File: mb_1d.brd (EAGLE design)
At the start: 100 x 80 mm, 59 parts, among them CON1 1013279X_AMPHENOL_2X25, CON2 1013279X_AMPHENOL_2X25, U1 TPS61040, U10 TPS610981, U2 MAX5394, U3 TPS61040, U5 RFD77101, U6 MAX5394, U7 MAX5026EUT+T, U8 MAX5394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

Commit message: Ground pour completed
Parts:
- moved R26 1.64 mm to (52.1, 47.8)
- moved R11 0.75 mm to (71.6, 27.6), turned to 90 degrees
- moved R12 0.61 mm to (60.1, 54.7)
- moved C12 0.41 mm to (66.4, 27.6), turned to 270 degrees
- moved R10 0.17 mm to (68.8, 27.9)
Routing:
- net GND: track 0.00 -> 46.3 mm, vias 0 -> 24
- net SCK: track 46.8 -> 48.4 mm
- net FB: track 16.7 -> 15.4 mm
- net VLDO: track 3.35 -> 4.62 mm
- net SS_POT1: track 4.19 -> 5.30 mm
- net RSTB_M: track 37.8 -> 38.5 mm
- net SCK_LS: track 21.6 -> 22.1 mm
- net SDI_LS: track 24.2 -> 23.6 mm
- added copper zone on layer 1, net GND
- added copper zone on layer 16, net GND

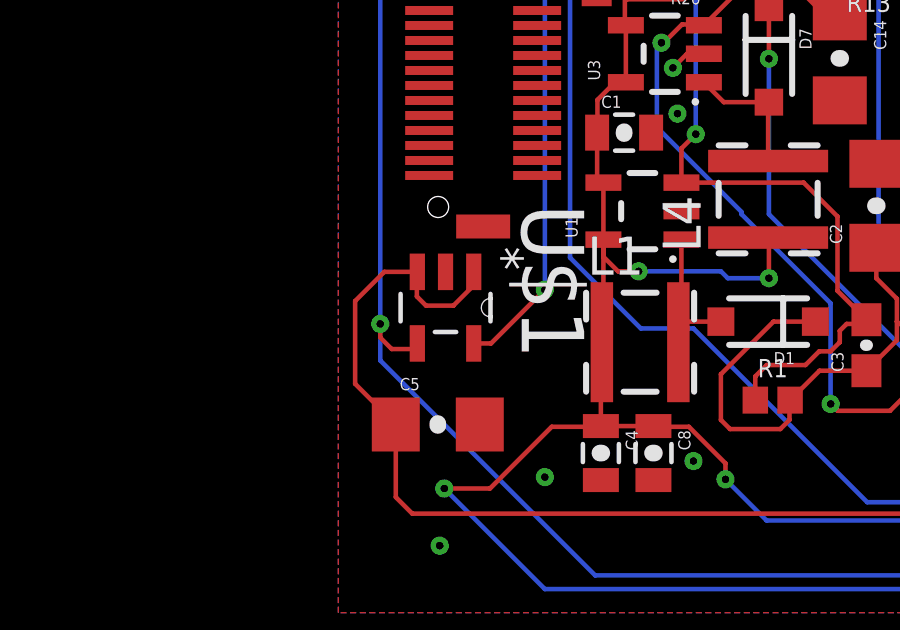
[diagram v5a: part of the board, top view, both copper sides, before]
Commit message: Fixed LT3014 error
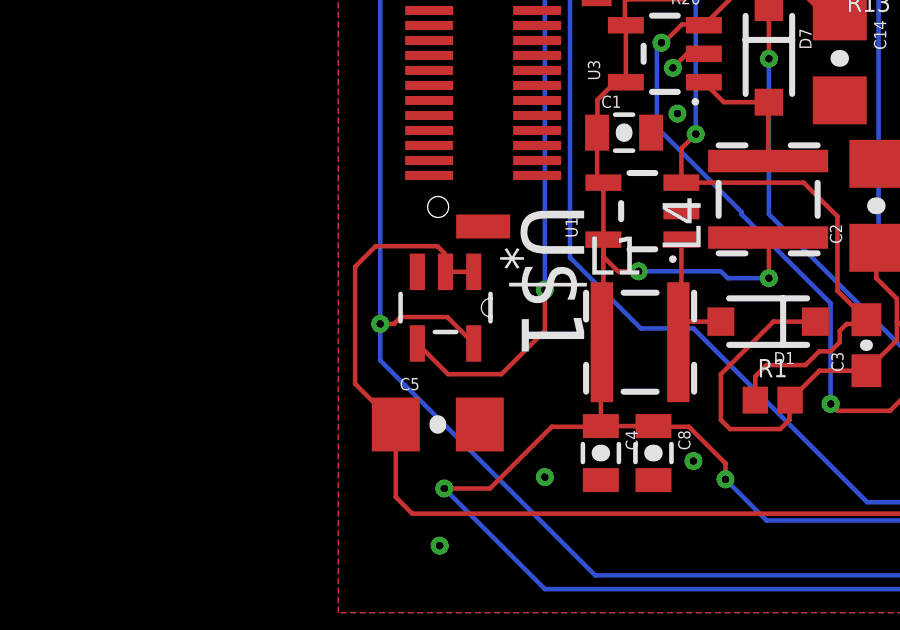
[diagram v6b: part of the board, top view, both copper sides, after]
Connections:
- net 50V: now also U$1.2; no longer U$1.3
- net ADJ: now also U$1.4; no longer U$1.5
- net GND: now also U$1.3; no longer U$1.2
- net HVDC: now also U$1.5; no longer U$1.4
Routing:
- net ADJ: track 37.4 -> 41.0 mm
- net HVDC: track 86.7 -> 88.3 mm
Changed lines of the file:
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@@
 <contactref element="U2" pad="2"/>
 <contactref element="R2" pad="1"/>
-<contactref element="U$1" pad="2"/>
+<contactref element="U$1" pad="3"/>
 <contactref element="C5" pad="2"/>
 <contactref element="U6" pad="2"/>
@@
 <signal name="HVDC">
 <contactref element="CON2" pad="32"/>
-<contactref element="U$1" pad="4"/>
+<contactref element="U$1" pad="5"/>
 <contactref element="R8" pad="1"/>
 <contactref element="C17" pad="2"/>
@@
 <wire x1="42.291" y1="55.245" x2="42.291" y2="36.0426" width="0.1524" layer="16"/>
 <via x="42.291" y="36.0426" extent="1-16" drill="0.254" diameter="0.381"/>
-<wire x1="42.291" y1="36.0426" x2="42.291" y2="35.5854" width="0.1524" layer="1"/>
-<wire x1="42.291" y1="35.5854" x2="42.672" y2="35.2044" width="0.1524" layer="1"/>
-<wire x1="42.672" y1="35.2044" x2="43.34" y2="35.2044" width="0.1524" layer="1"/>
-<wire x1="43.34" y1="35.2044" x2="43.5265" y2="35.3909" width="0.1524" layer="1"/>
 <wire x1="46.6132" y1="57.2516" x2="46.6132" y2="55.9435" width="0.1524" layer="1"/>
 <wire x1="46.6132" y1="55.9435" x2="46.5878" y2="55.9181" width="0.1524" layer="1"/>
@@
 <wire x1="49.4538" y1="27.6606" x2="42.291" y2="34.8234" width="0.1524" layer="16"/>
 <wire x1="42.291" y1="34.8234" x2="42.291" y2="36.0426" width="0.1524" layer="16"/>
+<wire x1="42.291" y1="36.0426" x2="42.7482" y2="36.0426" width="0.1524" layer="1"/>
+<wire x1="42.7482" y1="36.0426" x2="42.9768" y2="36.2712" width="0.1524" layer="1"/>
+<wire x1="42.9768" y1="36.2712" x2="44.5258" y2="36.2712" width="0.1524" layer="1"/>
+<wire x1="44.5258" y1="36.2712" x2="45.4061" y2="35.3909" width="0.1524" layer="1"/>
 </signal>
 <signal name="RESET">
@@
 <contactref element="R5" pad="2"/>
 <contactref element="U$1" pad="1"/>
-<contactref element="U$1" pad="3"/>
+<contactref element="U$1" pad="2"/>
 <contactref element="C5" pad="1"/>
 <wire x1="45.4061" y1="37.7785" x2="45.4061" y2="37.3289" width="0.1524" layer="1"/>
-<wire x1="45.4061" y1="37.3289" x2="44.7294" y2="36.6522" width="0.1524" layer="1"/>
-<wire x1="44.7294" y1="36.6522" x2="43.815" y2="36.6522" width="0.1524" layer="1"/>
-<wire x1="43.815" y1="36.6522" x2="43.5102" y2="36.957" width="0.1524" layer="1"/>
-<wire x1="43.5102" y1="36.957" x2="43.5102" y2="37.7622" width="0.1524" layer="1"/>
-<wire x1="43.5102" y1="37.7622" x2="43.5265" y2="37.7785" width="0.1524" layer="1"/>
-<wire x1="43.5265" y1="37.7785" x2="42.4267" y2="37.7785" width="0.1524" layer="1"/>
-<wire x1="42.4267" y1="37.7785" x2="41.4528" y2="36.8046" width="0.1524" layer="1"/>
-<wire x1="41.4528" y1="36.8046" x2="41.4528" y2="34.0457" width="0.1524" layer="1"/>
+<wire x1="41.4528" y1="37.9476" x2="41.4528" y2="34.0457" width="0.1524" layer="1"/>
 <wire x1="41.4528" y1="34.0457" x2="42.8087" y2="32.6898" width="0.1524" layer="1"/>
 <wire x1="42.8087" y1="32.6898" x2="42.8087" y2="30.2671" width="0.1524" layer="1"/>
@@
 <wire x1="65.9342" y1="28.2152" x2="64.6938" y2="26.9748" width="0.1524" layer="1"/>
 <wire x1="64.6938" y1="26.9748" x2="64.1604" y2="26.9748" width="0.1524" layer="1"/>
+<wire x1="41.4528" y1="37.9476" x2="42.1386" y2="38.6334" width="0.1524" layer="1"/>
+<wire x1="42.1386" y1="38.6334" x2="44.196" y2="38.6334" width="0.1524" layer="1"/>
+<wire x1="44.196" y1="38.6334" x2="44.4246" y2="38.4048" width="0.1524" layer="1"/>
+<wire x1="44.4246" y1="38.4048" x2="44.4246" y2="37.8202" width="0.1524" layer="1"/>
+<wire x1="44.4246" y1="37.8202" x2="44.4663" y2="37.7785" width="0.1524" layer="1"/>
+<wire x1="45.4061" y1="37.7785" x2="44.4663" y2="37.7785" width="0.1524" layer="1"/>
 </signal>
 <signal name="FB">
@@
 </signal>
 <signal name="ADJ">
-<contactref element="U$1" pad="5"/>
+<contactref element="U$1" pad="4"/>
 <contactref element="R8" pad="2"/>
 <contactref element="U6" pad="8"/>
 <contactref element="U6" pad="7"/>
 <wire x1="56.4902" y1="54.9522" x2="56.4902" y2="55.4522" width="0.1524" layer="1"/>
-<wire x1="45.4061" y1="35.3909" x2="45.9827" y2="35.3909" width="0.1524" layer="1"/>
-<wire x1="45.9827" y1="35.3909" x2="47.7774" y2="37.1856" width="0.1524" layer="1"/>
 <via x="47.7774" y="37.1856" extent="1-16" drill="0.254" diameter="0.381"/>
 <wire x1="47.7774" y1="37.1856" x2="47.7774" y2="54.102" width="0.1524" layer="16"/>
@@
 <wire x1="48.4632" y1="55.9308" x2="47.7605" y2="55.9308" width="0.1524" layer="1"/>
 <wire x1="47.7605" y1="55.9308" x2="47.7478" y2="55.9181" width="0.1524" layer="1"/>
+<wire x1="47.7774" y1="37.1856" x2="47.7774" y2="35.814" width="0.1524" layer="1"/>
+<wire x1="47.7774" y1="35.814" x2="46.3296" y2="34.3662" width="0.1524" layer="1"/>
+<wire x1="46.3296" y1="34.3662" x2="44.5512" y2="34.3662" width="0.1524" layer="1"/>
+<wire x1="44.5512" y1="34.3662" x2="43.5265" y2="35.3909" width="0.1524" layer="1"/>
 </signal>
 <signal name="N$13">
